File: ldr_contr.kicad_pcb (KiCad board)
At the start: 2 copper layers, 95.2 x 97 mm, 21 parts, among them P1 CONN_01X03, P2 CONN_01X04, P3 CONN_02X17, U1 ADG728, U2 ADG728, U3 ADG728, U4 PCA9306, U5 LM317_3PinPackage

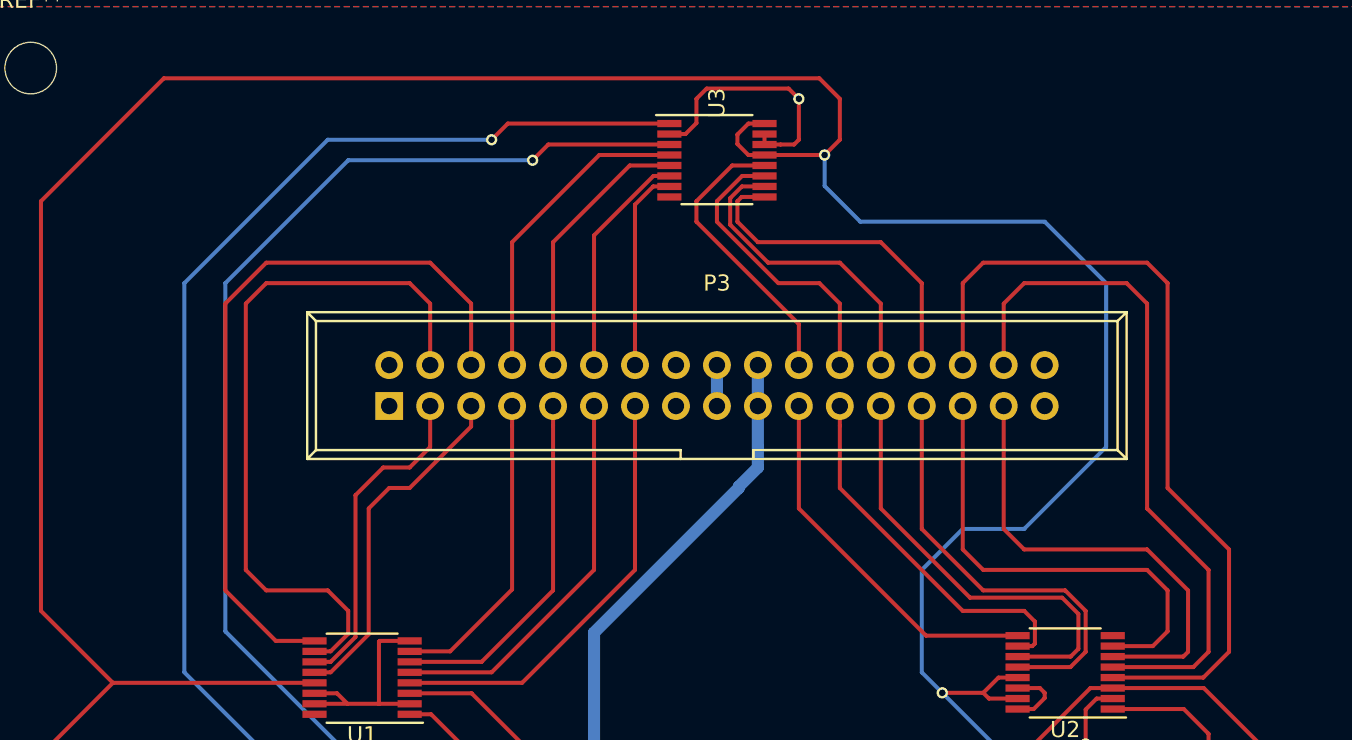
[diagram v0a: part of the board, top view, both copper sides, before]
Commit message: fixed adg728 airwire for the D input to ground
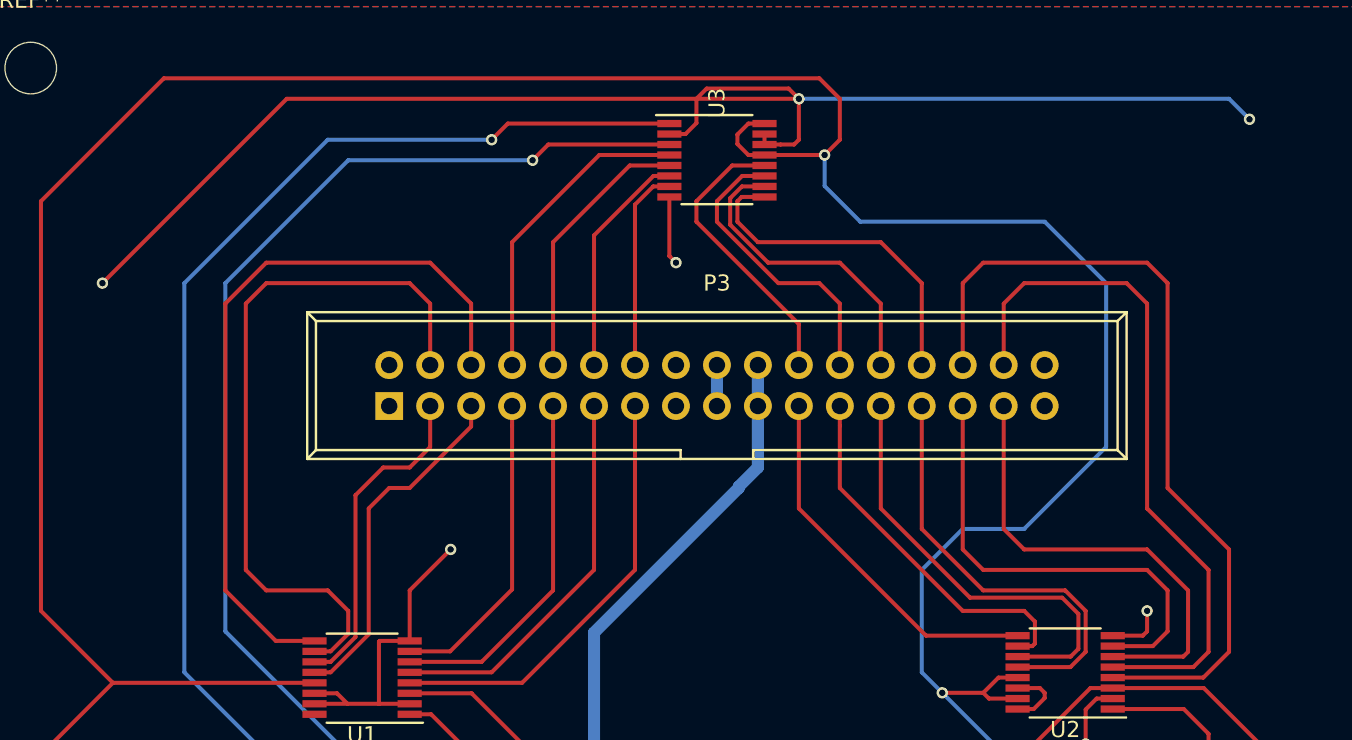
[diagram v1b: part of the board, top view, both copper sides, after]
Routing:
- net GND: track 49.4 -> 140.3 mm, vias 3 -> 8
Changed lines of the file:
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@@
-(kicad_pcb (version 4) (host pcbnew 4.0.7)
+(kicad_pcb (version 4) (host pcbnew 4.0.7-e2-6376~58~ubuntu16.04.1)
   (general
     (links 77)
-    (no_connects 2)
+    (no_connects 0)
     (area 123.157857 61.5 228.632143 160.215)
     (thickness 1.6)
     (drawings 4)
-    (tracks 343)
+    (tracks 359)
     (zones 0)
     (modules 21)
@@
   (gr_line (start 128.27 159.25) (end 223.52 159.25) (angle 90) (layer Edge.Cuts) (width 0.15))
   (gr_line (start 128.27 62.23) (end 223.52 62.23) (angle 90) (layer Edge.Cuts) (width 0.15))
+  (via (at 208.28 69.85) (size 0.7) (drill 0.4) (layers F.Cu B.Cu) (net 1))
+  (segment (start 207.01 68.58) (end 208.28 69.85) (width 0.25) (layer B.Cu) (net 1))
+  (segment (start 180.34 68.58) (end 207.01 68.58) (width 0.25) (layer B.Cu) (net 1))
+  (via (at 137.16 80.01) (size 0.7) (drill 0.4) (layers F.Cu B.Cu) (net 1))
+  (segment (start 148.59 68.58) (end 137.16 80.01) (width 0.25) (layer F.Cu) (net 1))
+  (segment (start 180.34 68.58) (end 148.59 68.58) (width 0.25) (layer F.Cu) (net 1))
+  (via (at 158.75 96.52) (size 0.7) (drill 0.4) (layers F.Cu B.Cu) (net 1))
+  (segment (start 156.21 99.06) (end 158.75 96.52) (width 0.25) (layer F.Cu) (net 1))
+  (segment (start 156.21 102.19) (end 156.21 99.06) (width 0.25) (layer F.Cu) (net 1))
+  (via (at 172.72 78.74) (size 0.7) (drill 0.4) (layers F.Cu B.Cu) (net 1))
+  (segment (start 172.31 78.33) (end 172.72 78.74) (width 0.25) (layer F.Cu) (net 1))
+  (segment (start 172.31 74.665) (end 172.31 78.33) (width 0.25) (layer F.Cu) (net 1))
+  (via (at 201.93 100.33) (size 0.7) (drill 0.4) (layers F.Cu B.Cu) (net 1))
+  (segment (start 201.93 101.6) (end 201.93 100.33) (width 0.25) (layer F.Cu) (net 1))
+  (segment (start 201.665 101.865) (end 201.93 101.6) (width 0.25) (layer F.Cu) (net 1))
+  (segment (start 199.8 101.865) (end 201.665 101.865) (width 0.25) (layer F.Cu) (net 1))
   (via (at 180.34 68.58) (size 0.7) (drill 0.4) (layers F.Cu B.Cu) (net 1))
   (segment (start 178.21 71.415) (end 178.21 70.765) (width 0.25) (layer F.Cu) (net 1))

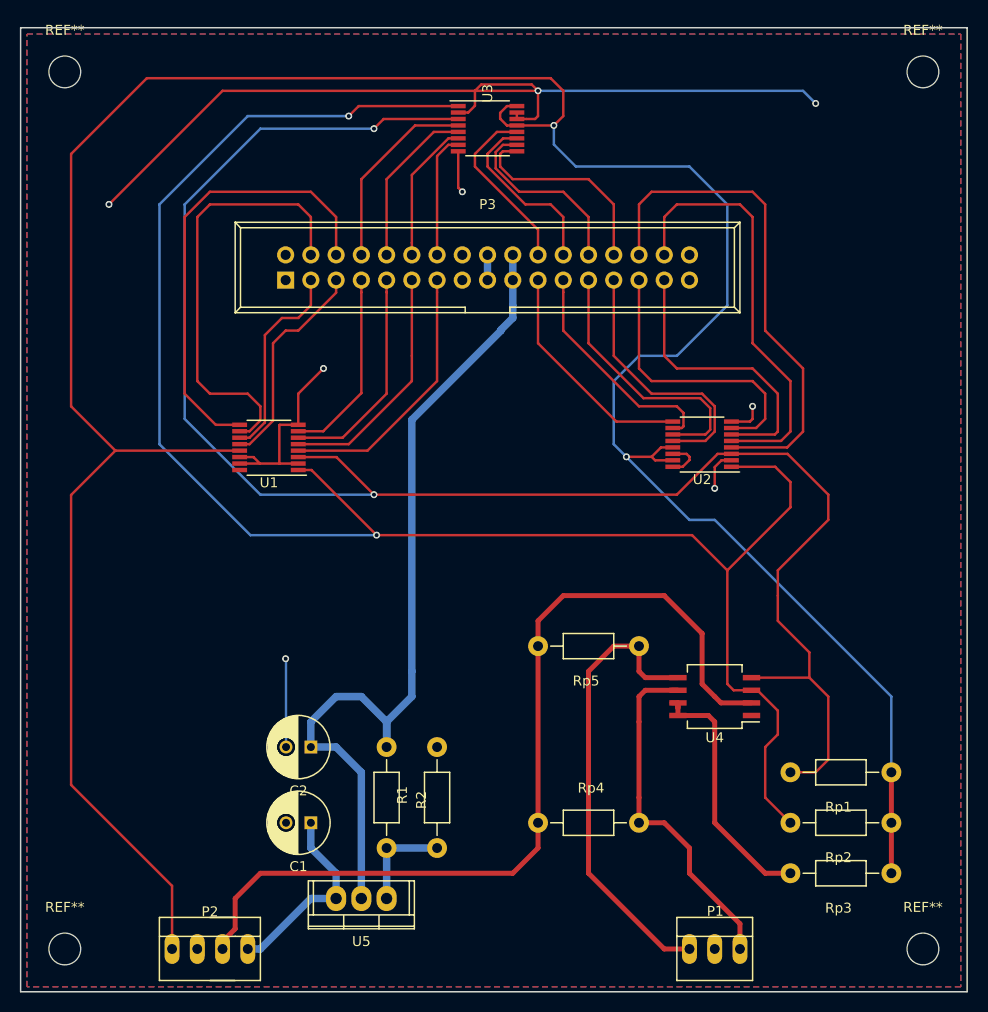
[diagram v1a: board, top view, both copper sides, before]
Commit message: Minor fix for 5V power line
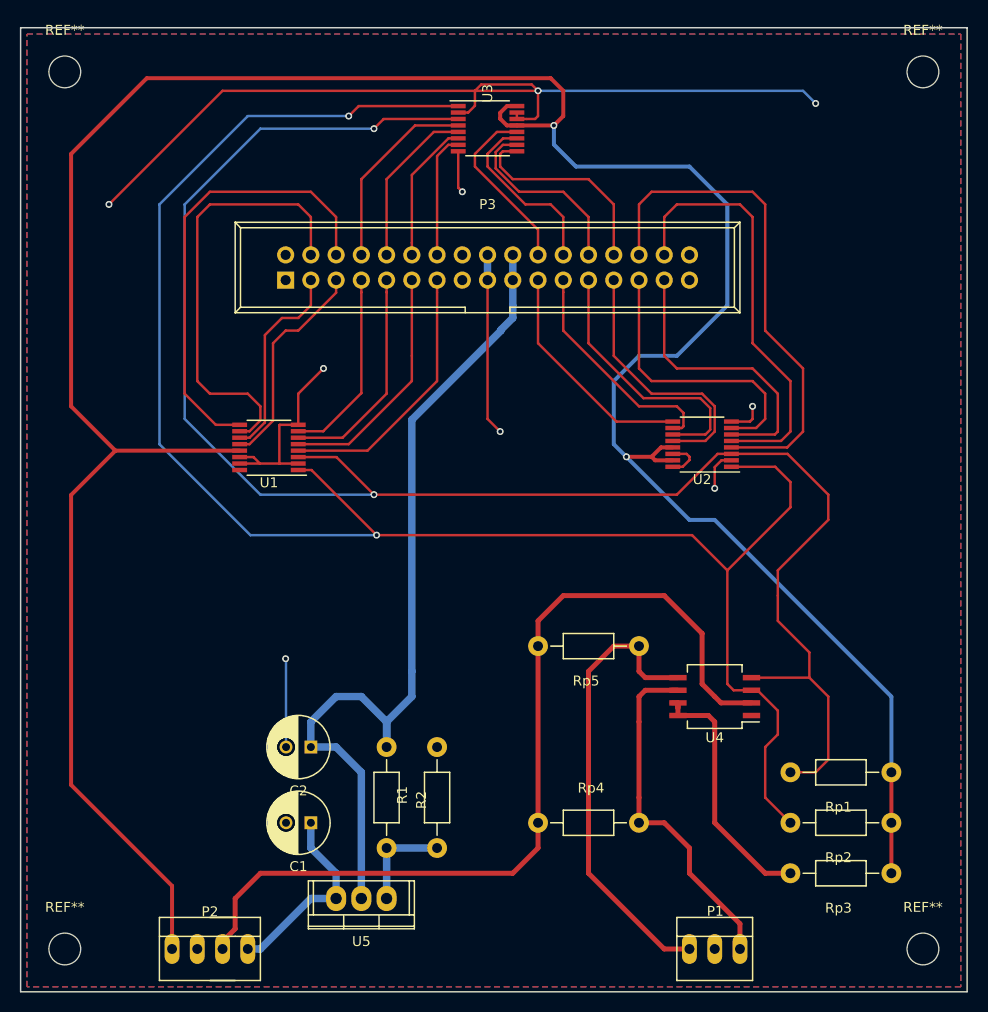
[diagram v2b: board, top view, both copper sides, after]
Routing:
- net GND: track 140.3 -> 156.0 mm, vias 8 -> 9
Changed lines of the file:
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@@
     (thickness 1.6)
     (drawings 4)
-    (tracks 359)
+    (tracks 362)
     (zones 0)
     (modules 21)
@@
   (gr_line (start 128.27 159.25) (end 223.52 159.25) (angle 90) (layer Edge.Cuts) (width 0.15))
   (gr_line (start 128.27 62.23) (end 223.52 62.23) (angle 90) (layer Edge.Cuts) (width 0.15))
+  (via (at 176.53 102.87) (size 0.7) (drill 0.4) (layers F.Cu B.Cu) (net 1))
+  (segment (start 175.26 101.6) (end 176.53 102.87) (width 0.25) (layer F.Cu) (net 1))
+  (segment (start 175.26 87.63) (end 175.26 101.6) (width 0.25) (layer F.Cu) (net 1))
   (via (at 208.28 69.85) (size 0.7) (drill 0.4) (layers F.Cu B.Cu) (net 1))
   (segment (start 207.01 68.58) (end 208.28 69.85) (width 0.25) (layer B.Cu) (net 1))
@@
   (segment (start 200.66 152.4) (end 195.58 147.32) (width 0.5) (layer F.Cu) (net 4))
   (segment (start 200.66 154.94) (end 200.66 152.4) (width 0.5) (layer F.Cu) (net 4))
-  (segment (start 198.12 111.76) (end 195.58 111.76) (width 0.25) (layer B.Cu) (net 5))
-  (segment (start 195.58 111.76) (end 189.23 105.41) (width 0.25) (layer B.Cu) (net 5))
-  (segment (start 215.9 129.54) (end 198.12 111.76) (width 0.25) (layer B.Cu) (net 5))
-  (segment (start 215.9 137.16) (end 215.9 129.54) (width 0.25) (layer B.Cu) (net 5))
-  (segment (start 187.96 97.79) (end 187.96 104.14) (width 0.25) (layer B.Cu) (net 5))
-  (segment (start 187.96 104.14) (end 189.23 105.41) (width 0.25) (layer B.Cu) (net 5))
-  (segment (start 190.5 95.25) (end 187.96 97.79) (width 0.25) (layer B.Cu) (net 5))
-  (segment (start 194.31 95.25) (end 190.5 95.25) (width 0.25) (layer B.Cu) (net 5))
-  (segment (start 199.39 90.17) (end 194.31 95.25) (width 0.25) (layer B.Cu) (net 5))
-  (segment (start 199.39 80.01) (end 199.39 90.17) (width 0.25) (layer B.Cu) (net 5))
-  (segment (start 195.58 76.2) (end 199.39 80.01) (width 0.25) (layer B.Cu) (net 5))
-  (segment (start 184.15 76.2) (end 195.58 76.2) (width 0.25) (layer B.Cu) (net 5))
-  (segment (start 181.935 73.985) (end 184.15 76.2) (width 0.25) (layer B.Cu) (net 5))
-  (segment (start 181.935 72.065) (end 181.935 73.985) (width 0.25) (layer B.Cu) (net 5))
+  (segment (start 198.12 111.76) (end 195.58 111.76) (width 0.4) (layer B.Cu) (net 5))
+  (segment (start 195.58 111.76) (end 189.23 105.41) (width 0.4) (layer B.Cu) (net 5))
+  (segment (start 215.9 129.54) (end 198.12 111.76) (width 0.4) (layer B.Cu) (net 5))
+  (segment (start 215.9 137.16) (end 215.9 129.54) (width 0.4) (layer B.Cu) (net 5))
+  (segment (start 187.96 97.79) (end 187.96 104.14) (width 0.4) (layer B.Cu) (net 5))
+  (segment (start 187.96 104.14) (end 189.23 105.41) (width 0.4) (layer B.Cu) (net 5))
+  (segment (start 190.5 95.25) (end 187.96 97.79) (width 0.4) (layer B.Cu) (net 5))
+  (segment (start 194.31 95.25) (end 190.5 95.25) (width 0.4) (layer B.Cu) (net 5))
+  (segment (start 199.39 90.17) (end 194.31 95.25) (width 0.4) (layer B.Cu) (net 5))
+  (segment (start 199.39 80.01) (end 199.39 90.17) (width 0.4) (layer B.Cu) (net 5))
+  (segment (start 195.58 76.2) (end 199.39 80.01) (width 0.4) (layer B.Cu) (net 5))
+  (segment (start 184.15 76.2) (end 195.58 76.2) (width 0.4) (layer B.Cu) (net 5))
+  (segment (start 181.935 73.985) (end 184.15 76.2) (width 0.4) (layer B.Cu) (net 5))
+  (segment (start 181.935 72.065) (end 181.935 73.985) (width 0.4) (layer B.Cu) (net 5))
   (via (at 181.935 72.065) (size 0.7) (drill 0.4) (layers F.Cu B.Cu) (net 5))
   (via (at 189.23 105.41) (size 0.7) (drill 0.4) (layers F.Cu B.Cu) (net 5))
-  (segment (start 191.77 105.41) (end 189.23 105.41) (width 0.25) (layer F.Cu) (net 5))
-  (segment (start 192.715 104.465) (end 191.77 105.41) (width 0.25) (layer F.Cu) (net 5))
-  (segment (start 193.9 104.465) (end 192.715 104.465) (width 0.25) (layer F.Cu) (net 5))
-  (segment (start 192.125 105.765) (end 191.77 105.41) (width 0.25) (layer F.Cu) (net 5))
-  (segment (start 193.9 105.765) (end 192.125 105.765) (width 0.25) (layer F.Cu) (net 5))
-  (segment (start 137.81 104.79) (end 133.35 100.33) (width 0.25) (layer F.Cu) (net 5))
-  (segment (start 133.35 100.33) (end 133.35 74.93) (width 0.25) (layer F.Cu) (net 5))
-  (segment (start 133.35 74.93) (end 140.97 67.31) (width 0.25) (layer F.Cu) (net 5))
-  (segment (start 140.97 67.31) (end 181.61 67.31) (width 0.25) (layer F.Cu) (net 5))
-  (segment (start 181.61 67.31) (end 182.88 68.58) (width 0.25) (layer F.Cu) (net 5))
-  (segment (start 182.88 68.58) (end 182.88 71.12) (width 0.25) (layer F.Cu) (net 5))
-  (segment (start 181.935 72.065) (end 178.21 72.065) (width 0.25) (layer F.Cu) (net 5))
-  (segment (start 182.88 71.12) (end 181.935 72.065) (width 0.25) (layer F.Cu) (net 5))
-  (segment (start 150.31 104.79) (end 137.81 104.79) (width 0.25) (layer F.Cu) (net 5))
-  (segment (start 137.81 104.79) (end 133.35 109.25) (width 0.25) (layer F.Cu) (net 5))
-  (segment (start 133.35 109.25) (end 133.35 138.43) (width 0.25) (layer F.Cu) (net 5))
-  (segment (start 133.35 138.43) (end 143.51 148.59) (width 0.25) (layer F.Cu) (net 5))
-  (segment (start 143.51 148.59) (end 143.51 154.94) (width 0.25) (layer F.Cu) (net 5))
-  (segment (start 176.53 70.795) (end 176.53 71.385) (width 0.25) (layer F.Cu) (net 5))
-  (segment (start 176.53 71.385) (end 177.21 72.065) (width 0.25) (layer F.Cu) (net 5))
-  (segment (start 177.21 72.065) (end 178.21 72.065) (width 0.25) (layer F.Cu) (net 5))
-  (segment (start 178.21 70.115) (end 177.21 70.115) (width 0.25) (layer F.Cu) (net 5))
-  (segment (start 177.21 70.115) (end 176.53 70.795) (width 0.25) (layer F.Cu) (net 5))
-  (segment (start 215.9 142.24) (end 215.9 137.16) (width 0.5) (layer F.Cu) (net 5))
-  (segment (start 215.9 147.32) (end 215.9 142.24) (width 0.5) (layer F.Cu) (net 5))
+  (segment (start 191.77 105.41) (end 189.23 105.41) (width 0.4) (layer F.Cu) (net 5))
+  (segment (start 192.715 104.465) (end 191.77 105.41) (width 0.4) (layer F.Cu) (net 5))
+  (segment (start 193.9 104.465) (end 192.715 104.465) (width 0.4) (layer F.Cu) (net 5))
+  (segment (start 192.125 105.765) (end 191.77 105.41) (width 0.4) (layer F.Cu) (net 5))
+  (segment (start 193.9 105.765) (end 192.125 105.765) (width 0.4) (layer F.Cu) (net 5))
+  (segment (start 137.81 104.79) (end 133.35 100.33) (width 0.4) (layer F.Cu) (net 5))
+  (segment (start 133.35 100.33) (end 133.35 74.93) (width 0.4) (layer F.Cu) (net 5))
+  (segment (start 133.35 74.93) (end 140.97 67.31) (width 0.4) (layer F.Cu) (net 5))
+  (segment (start 140.97 67.31) (end 181.61 67.31) (width 0.4) (layer F.Cu) (net 5))
+  (segment (start 181.61 67.31) (end 182.88 68.58) (width 0.4) (layer F.Cu) (net 5))
+  (segment (start 182.88 68.58) (end 182.88 71.12) (width 0.4) (layer F.Cu) (net 5))
+  (segment (start 181.935 72.065) (end 178.21 72.065) (width 0.4) (layer F.Cu) (net 5))
+  (segment (start 182.88 71.12) (end 181.935 72.065) (width 0.4) (layer F.Cu) (net 5))
+  (segment (start 150.31 104.79) (end 137.81 104.79) (width 0.4) (layer F.Cu) (net 5))
+  (segment (start 137.81 104.79) (end 133.35 109.25) (width 0.4) (layer F.Cu) (net 5))
+  (segment (start 133.35 109.25) (end 133.35 138.43) (width 0.4) (layer F.Cu) (net 5))
+  (segment (start 133.35 138.43) (end 143.51 148.59) (width 0.4) (layer F.Cu) (net 5))
+  (segment (start 143.51 148.59) (end 143.51 154.94) (width 0.4) (layer F.Cu) (net 5))
+  (segment (start 176.53 70.795) (end 176.53 71.385) (width 0.4) (layer F.Cu) (net 5))
+  (segment (start 176.53 71.385) (end 177.21 72.065) (width 0.4) (layer F.Cu) (net 5))
+  (segment (start 177.21 72.065) (end 178.21 72.065) (width 0.4) (layer F.Cu) (net 5))
+  (segment (start 178.21 70.115) (end 177.21 70.115) (width 0.4) (layer F.Cu) (net 5))
+  (segment (start 177.21 70.115) (end 176.53 70.795) (width 0.4) (layer F.Cu) (net 5))
+  (segment (start 215.9 142.24) (end 215.9 137.16) (width 0.4) (layer F.Cu) (net 5))
+  (segment (start 215.9 147.32) (end 215.9 142.24) (width 0.4) (layer F.Cu) (net 5))
   (segment (start 198.12 129.54) (end 196.85 128.27) (width 0.5) (layer F.Cu) (net 6))
   (segment (start 196.85 123.19) (end 193.04 119.38) (width 0.5) (layer F.Cu) (net 6))
